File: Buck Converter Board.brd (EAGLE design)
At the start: 120.6 x 40.3 mm, 8 parts, among them J1 POWERPOLE_POWER25A_HORIZONTAL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, J2 POWERPOLE_POWER25A_HORIZONTAL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, J3 POWERPOLE_POWER25A_HORIZONTAL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

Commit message: added REV Logo, fixed some hidden airwires
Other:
- board text added: "Fuse 48V, 8A"
- board text removed: "48V, 10A Fuse"
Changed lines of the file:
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@@
 <?xml version="1.0" encoding="utf-8"?>
 <!DOCTYPE eagle SYSTEM "eagle.dtd">
-<eagle version="9.2.1">
+<eagle version="9.1.3">
 <drawing>
 <settings>
@@
 <setting verticaltext="up"/>
 </settings>
-<grid distance="50" unitdist="mil" unit="mil" style="lines" multiple="1" display="no" altdistance="5" altunitdist="mil" altunit="mil"/>
+<grid distance="0.03125" unitdist="mm" unit="mm" style="lines" multiple="1" display="no" altdistance="5" altunitdist="mil" altunit="mm"/>
 <layers>
 <layer number="1" name="Top" color="4" fill="1" visible="yes" active="yes"/>
@@
 <wire x1="15.24" y1="75.87" x2="15.24" y2="35.56" width="0" layer="20"/>
 <text x="25.4" y="66.04" size="1.778" layer="25" rot="R180">48V IN</text>
-<text x="44.45" y="71.12" size="1.778" layer="25" rot="R180">48V, 10A Fuse</text>
+<text x="39.35625" y="70.96375" size="1.016" layer="25" rot="R180">Fuse
+48V, 8A</text>
 <text x="128.27" y="72.39" size="1.778" layer="25" rot="R180">12V OUT</text>
 <text x="128.27" y="40.64" size="1.778" layer="25" rot="R180">12V OUT</text>
@@
 <vertex x="40.64" y="69.85"/>
 <vertex x="49.53" y="69.85" curve="-90"/>
-<vertex x="55.88" y="63.5"/>
-<vertex x="55.88" y="60.96" curve="-90"/>
-<vertex x="54.61" y="59.69"/>
+<vertex x="55.88" y="63.5" curve="-90"/>
+<vertex x="52.07" y="59.69"/>
 <vertex x="33.02" y="59.69" curve="-90"/>
 </polygon>
@@
 <signal name="BGND" airwireshidden="yes">
 <polygon width="0.1524" layer="16" isolate="0.254">
-<vertex x="55.88" y="43.18"/>
-<vertex x="55.88" y="59.69" curve="90"/>
-<vertex x="53.34" y="62.23"/>
+<vertex x="29.05" y="41.91"/>
+<vertex x="45.88" y="41.91" curve="90"/>
+<vertex x="55.88" y="51.91"/>
+<vertex x="55.88" y="52.23" curve="90"/>
+<vertex x="45.88" y="62.23"/>
 <vertex x="41.91" y="62.23"/>
-<vertex x="20.32" y="62.23" curve="90"/>
-<vertex x="19.05" y="60.96"/>
-<vertex x="19.05" y="45.72" curve="90"/>
-<vertex x="22.86" y="41.91"/>
-<vertex x="53.34" y="41.91" curve="90"/>
+<vertex x="29.05" y="62.23" curve="90"/>
+<vertex x="19.05" y="52.23"/>
+<vertex x="19.05" y="51.91" curve="90"/>
 </polygon>
 <contactref element="J1" pad="BLACK"/>
@@
 <polygon width="0.1524" layer="1">
 <vertex x="101.6" y="59.69"/>
-<vertex x="101.6" y="67.31" curve="-90"/>
-<vertex x="105.41" y="71.12"/>
-<vertex x="125.73" y="71.12" curve="-90"/>
-<vertex x="130.81" y="66.04"/>
-<vertex x="130.81" y="44.45" curve="-90"/>
-<vertex x="127" y="40.64"/>
-<vertex x="106.68" y="40.64" curve="-90"/>
-<vertex x="101.6" y="45.72"/>
+<vertex x="101.6" y="61.12" curve="-90"/>
+<vertex x="111.6" y="71.12"/>
+<vertex x="120.81" y="71.12" curve="-90"/>
+<vertex x="130.81" y="61.12"/>
+<vertex x="130.81" y="50.64" curve="-90"/>
+<vertex x="120.81" y="40.64"/>
+<vertex x="111.6" y="40.64" curve="-90"/>
+<vertex x="101.6" y="50.64"/>
 </polygon>
 </signal>
@@
 <contactref element="D1" pad="A"/>
 <polygon width="0.1524" layer="16">
-<vertex x="101.6" y="67.31" curve="-90"/>
-<vertex x="105.41" y="71.12"/>
-<vertex x="125.73" y="71.12" curve="-90"/>
-<vertex x="130.81" y="66.04"/>
-<vertex x="130.81" y="44.45" curve="-90"/>
-<vertex x="127" y="40.64"/>
-<vertex x="106.68" y="40.64" curve="-90"/>
-<vertex x="101.6" y="45.72"/>
 <vertex x="101.6" y="60.96"/>
+<vertex x="101.6" y="61.12" curve="-90"/>
+<vertex x="111.6" y="71.12"/>
+<vertex x="120.81" y="71.12" curve="-90"/>
+<vertex x="130.81" y="61.12"/>
+<vertex x="130.81" y="50.64" curve="-90"/>
+<vertex x="120.81" y="40.64"/>
+<vertex x="111.6" y="40.64" curve="-90"/>
+<vertex x="101.6" y="50.64"/>
 </polygon>
 <wire x1="120.31" y1="53.34" x2="117.79" y2="58.42" width="0" layer="19" extent="1-1"/>
@@
 </drawing>
 <compatibility>
+<note version="6.3" minversion="6.2.2" severity="warning">
+Since Version 6.2.2 text objects can contain more than one line,
+which will not be processed correctly with this version.
+</note>
 <note version="8.2" severity="warning">
 Since Version 8.2, EAGLE supports online libraries. The ids

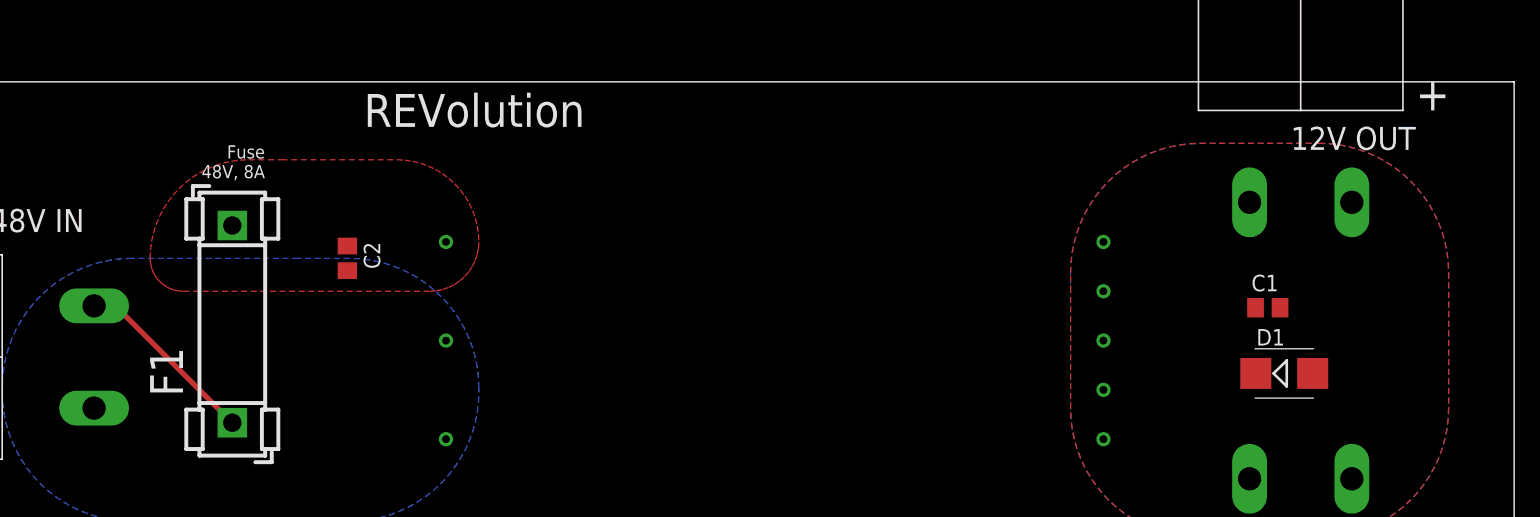
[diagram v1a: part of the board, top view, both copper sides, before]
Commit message: Changed diode package, made a trace larger
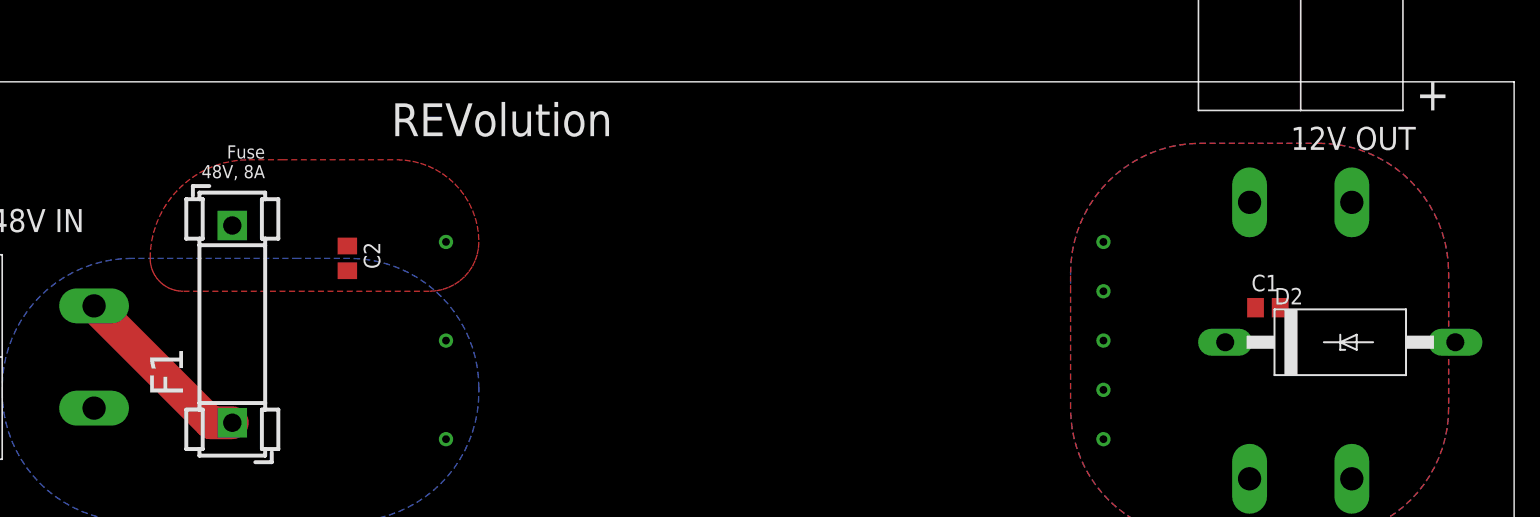
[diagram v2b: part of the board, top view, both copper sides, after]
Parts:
- removed D1: (no value), diode:SMB
- added D2: 15KEXX, diode:CB429-17
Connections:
- net OGND: now also D2.A; no longer D1.A
- net V_OUT: now also D2.C; no longer D1.C
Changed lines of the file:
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@@
 <?xml version="1.0" encoding="utf-8"?>
 <!DOCTYPE eagle SYSTEM "eagle.dtd">
-<eagle version="9.1.3">
+<eagle version="9.2.2">
 <drawing>
 <settings>
@@
 <text x="128.27" y="72.39" size="1.778" layer="25" rot="R180">12V OUT</text>
 <text x="128.27" y="40.64" size="1.778" layer="25" rot="R180">12V OUT</text>
-<text x="46.99" y="72.39" size="2.54" layer="25">REVolution</text>
+<text x="49.115" y="71.67125" size="2.54" layer="25">REVolution</text>
 </plain>
 <attributes>
@@
 <element name="J1" library="powerpoles" package="POWERPOLE_PAIR_25A_HORIZ_G2" value="POWERPOLE_POWER25A_HORIZONTAL_G2" x="19.05" y="54.61" smashed="yes" rot="R90"/>
 <element name="J2" library="powerpoles" package="POWERPOLE_PAIR_25A_HORIZ_G2" value="POWERPOLE_POWER25A_HORIZONTAL_G2" x="119.38" y="73.66" smashed="yes"/>
-<element name="D1" library="diode" library_urn="urn:adsk.eagle:library:210" package="SMB" package3d_urn="urn:adsk.eagle:package:43404/2" value="" x="118.11" y="53.34" smashed="yes">
-<attribute name="NAME" x="115.951" y="55.499" size="1.27" layer="25"/>
-<attribute name="VALUE" x="115.951" y="49.911" size="1.27" layer="27"/>
-</element>
 <element name="C2" library="rcl" library_urn="urn:adsk.eagle:library:334" package="C0805" package3d_urn="urn:adsk.eagle:package:23617/2" value="" x="45.72" y="62.23" smashed="yes" rot="R270">
 <attribute name="NAME" x="46.99" y="63.5" size="1.27" layer="25" rot="R270"/>
@@
 <element name="J3" library="powerpoles" package="POWERPOLE_PAIR_25A_HORIZ_G2" value="POWERPOLE_POWER25A_HORIZONTAL_G2" x="119.38" y="38.1" smashed="yes" rot="R180"/>
 <element name="UEE150W" library="REV Aux Circuit" package="DOSA1/8" value="UEE150W" x="49.53" y="44.45" smashed="yes"/>
+<element name="D2" library="diode" library_urn="urn:adsk.eagle:library:210" package="CB429-17" package3d_urn="urn:adsk.eagle:package:43360/1" value="15KEXX" x="122.4375" y="55.75" smashed="yes">
+<attribute name="NAME" x="117.3575" y="58.671" size="1.27" layer="25" ratio="10"/>
+<attribute name="VALUE" x="119.8975" y="53.591" size="1.27" layer="27" ratio="10"/>
+</element>
 </elements>
 <signals>
@@
 <contactref element="J1" pad="RED"/>
 <contactref element="F1" pad="1"/>
-<wire x1="26.15" y1="58.56" x2="27.8" y2="58.56" width="0.4064" layer="1"/>
-<wire x1="27.8" y1="58.56" x2="36.83" y2="49.53" width="0.4064" layer="1"/>
+<wire x1="26.15" y1="58.56" x2="35.18" y2="49.53" width="2.54" layer="1"/>
+<wire x1="35.18" y1="49.53" x2="36.83" y2="49.53" width="2.54" layer="1"/>
 </signal>
 <signal name="V_BATT_FUSED">
@@
 <contactref element="UEE150W" pad="V_OUT+"/>
 <contactref element="C1" pad="1"/>
-<contactref element="D1" pad="C"/>
 <polygon width="0.1524" layer="1">
 <vertex x="101.6" y="59.69"/>
@@
 <vertex x="101.6" y="50.64"/>
 </polygon>
+<contactref element="D2" pad="C"/>
 </signal>
 <signal name="OGND" airwireshidden="yes">
@@
 <contactref element="J3" pad="BLACK"/>
 <contactref element="UEE150W" pad="V_OUT-"/>
-<contactref element="D1" pad="A"/>
 <polygon width="0.1524" layer="16">
 <vertex x="101.6" y="60.96"/>
@@
 <vertex x="101.6" y="50.64"/>
 </polygon>
-<wire x1="120.31" y1="53.34" x2="117.79" y2="58.42" width="0" layer="19" extent="1-1"/>
+<contactref element="D2" pad="A"/>
 <wire x1="115.43" y1="66.56" x2="117.79" y2="58.42" width="0" layer="19" extent="1-1"/>
 </signal>

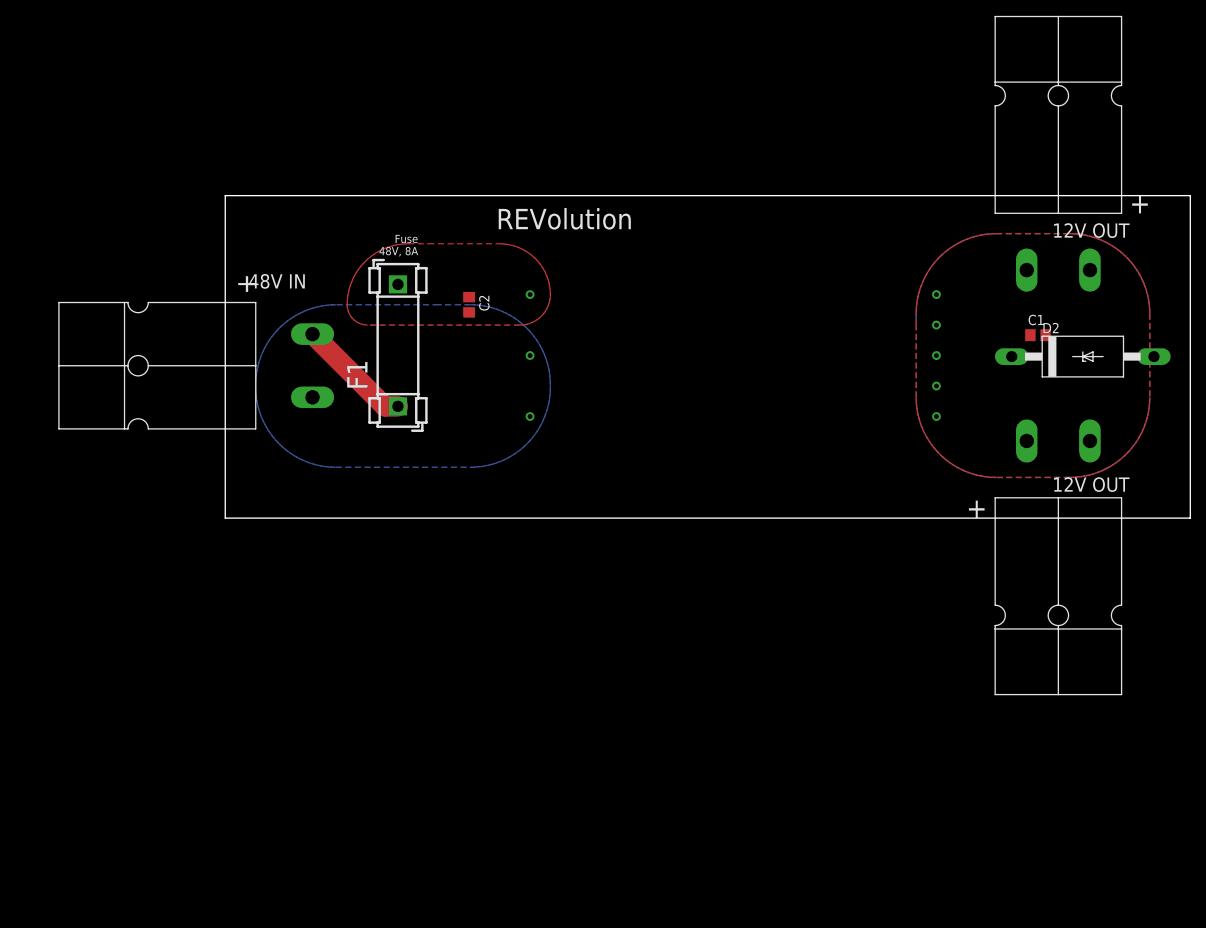
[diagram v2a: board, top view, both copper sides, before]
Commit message: fix planes, move connectors inwards, add REV logo
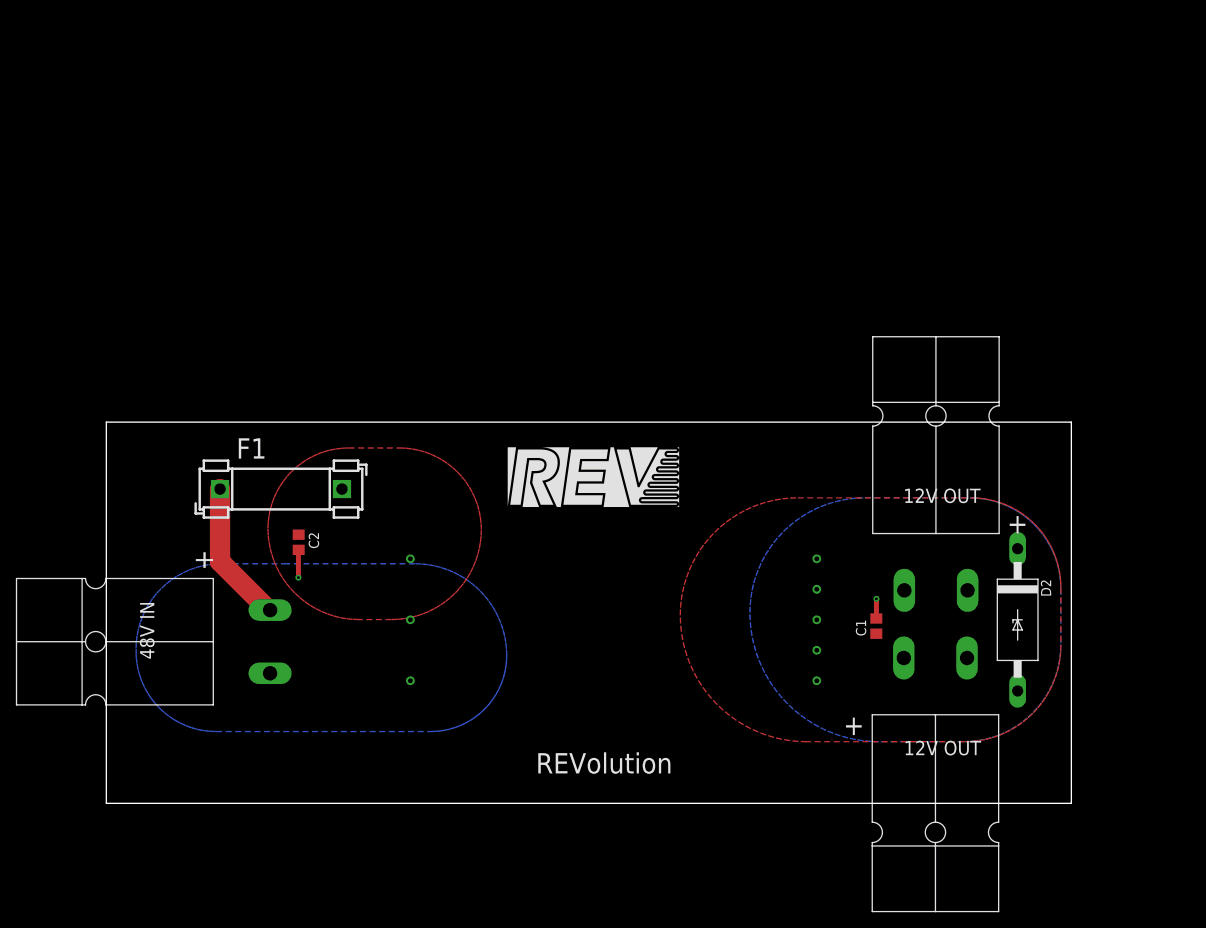
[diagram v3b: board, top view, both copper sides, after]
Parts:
- moved J2 42.9 mm to (104.1, 33.6)
- moved C1 41.6 mm to (96.6, 22.1), turned to 90 degrees
- moved C2 36.5 mm to (24.4, 32.5)
- moved UEE150W 36.3 mm to (34.6, 11.4)
- moved J1 34.9 mm to (13.7, 20.1)
- moved D2 33.9 mm to (114.3, 22.8), turned to 270 degrees
- moved J3 31.2 mm to (104.0, 11.0)
- moved F1 24.5 mm to (14.6, 39.2), turned to 0 degrees
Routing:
- net BGND: track 0.00 -> 3.48 mm, vias 0 -> 1
- net VBATT: track 14.4 -> 17.8 mm
- net OGND: track 0.00 -> 2.47 mm, vias 0 -> 1
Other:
- board size 120.6 x 40.3 mm -> 120.6 x 47.7 mm
- board text added: "/Users/louissmidt/Downloads/Untitled-1.BMP"
- board text removed: "Fuse 48V, 8A"

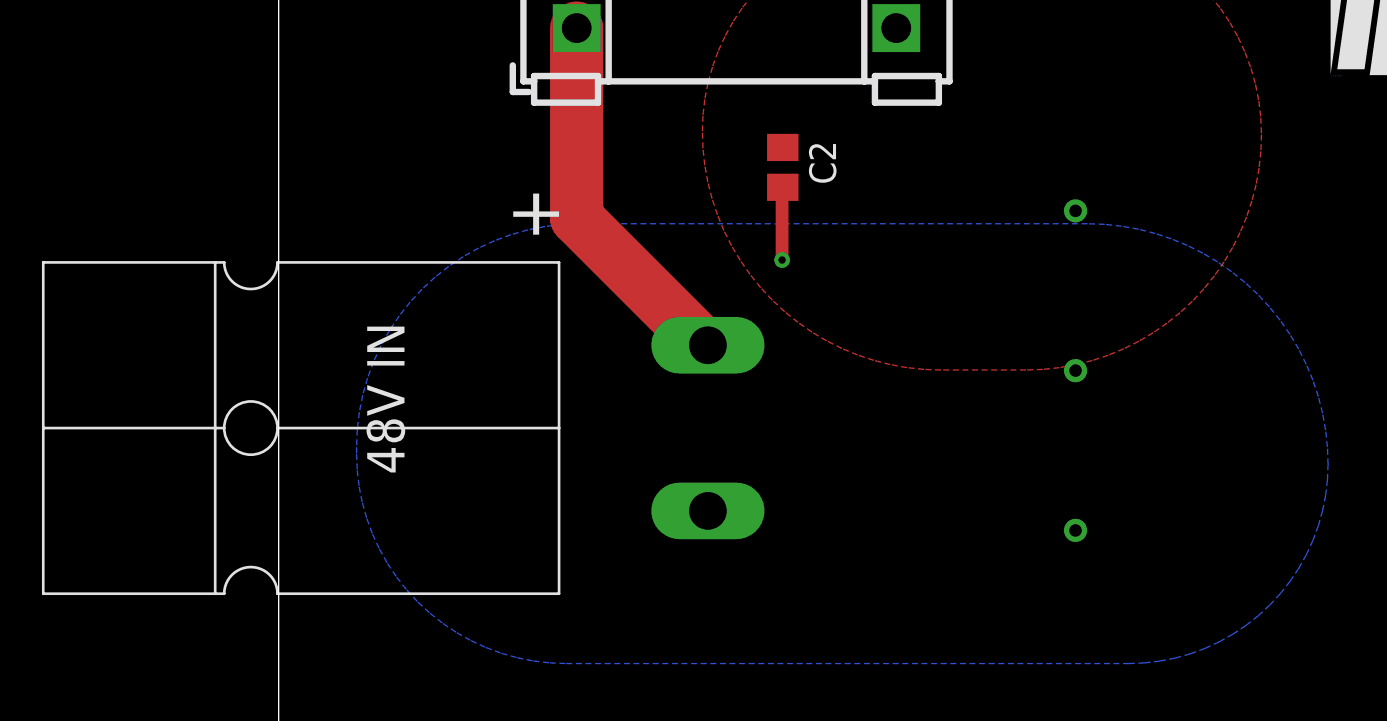
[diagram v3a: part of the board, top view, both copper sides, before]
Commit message: center input connector
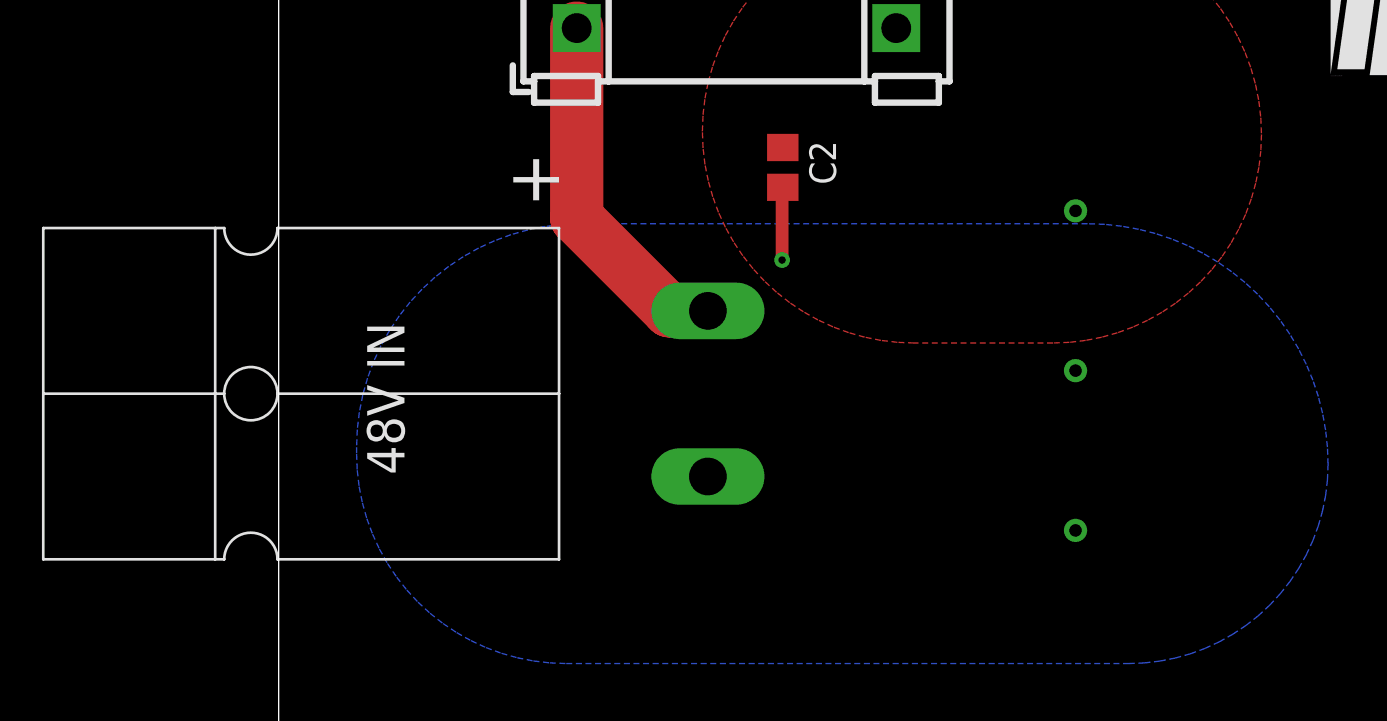
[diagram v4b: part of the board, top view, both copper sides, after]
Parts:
- moved J1 1.64 mm to (13.7, 21.8)
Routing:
- net VBATT: track 17.8 -> 17.1 mm
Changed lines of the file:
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@@
 <attribute name="OC_NEWARK" value="unknown" x="14.58875" y="39.1875" size="1.778" layer="27" display="off"/>
 </element>
-<element name="J1" library="powerpoles" package="POWERPOLE_PAIR_25A_HORIZ_G2" value="POWERPOLE_POWER25A_HORIZONTAL_G2" x="13.74625" y="20.11125" smashed="yes" rot="R90"/>
+<element name="J1" library="powerpoles" package="POWERPOLE_PAIR_25A_HORIZ_G2" value="POWERPOLE_POWER25A_HORIZONTAL_G2" x="13.74625" y="21.75125" smashed="yes" rot="R90"/>
 <element name="J2" library="powerpoles" package="POWERPOLE_PAIR_25A_HORIZ_G2" value="POWERPOLE_POWER25A_HORIZONTAL_G2" x="104.07625" y="33.63" smashed="yes"/>
 <element name="C2" library="rcl" library_urn="urn:adsk.eagle:library:334" package="C0805" package3d_urn="urn:adsk.eagle:package:23617/2" value="" x="24.41625" y="32.54375" smashed="yes" rot="R270">
@@
 <contactref element="F1" pad="1"/>
 <wire x1="14.58875" y1="39.1875" x2="14.58875" y2="30.13125" width="2.54" layer="1"/>
-<wire x1="20.65875" y1="24.06125" x2="14.58875" y2="30.13125" width="2.54" layer="1"/>
-<wire x1="20.84625" y1="24.06125" x2="20.65875" y2="24.06125" width="2.54" layer="1"/>
+<wire x1="19.01875" y1="25.70125" x2="14.58875" y2="30.13125" width="2.54" layer="1"/>
+<wire x1="20.84625" y1="25.70125" x2="19.01875" y2="25.70125" width="2.54" layer="1"/>
 </signal>
 <signal name="V_BATT_FUSED">
@@
 <vertex x="37.03125" y="44.3275" curve="-90"/>
 <vertex x="47.248125" y="34.110625" curve="-90"/>
-<vertex x="36.01625" y="22.87875"/>
-<vertex x="31.96625" y="22.87875" curve="-90"/>
+<vertex x="37.30625" y="24.16875"/>
+<vertex x="30.67625" y="24.16875" curve="-90"/>
 </polygon>
 </signal>
